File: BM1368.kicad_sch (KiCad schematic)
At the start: 38 parts, among them U2 BM1368_mode1, U9 BM1368_mode1

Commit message: Added 4th Phase Buck
Started to add 4th Phase for the Buck, implementing BM1370 footprint etc
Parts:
- removed U2, U9: BM1368_mode1, myfootprints:bm1368-package-modified, symbol mylib7:BM1368_mode1
- added U17, U2: BM1370_mode1, Nerd8:BM1370, symbol bitaxe:BM1370_mode1
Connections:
- net +0V8: now also U17.14 (VDDIO_08_0), U17.17 (VDDIO_08_1), U2.14 (VDDIO_08_0), U2.17 (VDDIO_08_1)
- net +1V2: now also U17.31 (VDD), U2.31 (VDD)
- net +1V8: now also U17.15 (VDDIO_12_0), U17.16 (VDDIO_12_1), U2.15 (VDDIO_12_0), U2.16 (VDDIO_12_1)
- net BI: now also U17.9 (BI)
- net BO: now also U2.22 (BO)
- net CI: now also U17.6 (CI)
- net CLKI: now also U17.8 (CLKI)
- net CLKO: now also U2.23 (CLKO)
- net CO: now also U2.25 (CO)
- net GND: now also U17.13 (PLL_VSS), U17.18 (VSS), U17.27 (VSS), U17.32 (VSS), U17.4 (VSS), U2.13 (PLL_VSS), U2.18 (VSS), U2.27 (VSS), U2.32 (VSS), U2.4 (VSS)
- net NRSTI: now also U17.5 (NRSTI)
- net NRSTO: now also U2.26 (NRSTO)
- net RI: now also U2.24 (RI)
- net RO: now also U17.7 (RO)
- net U9-VDD1_1: now also U2.28 (VDD1_1)
- net U9-VDD2_1: now also U2.29 (VDD2_1)
- net U9-VDD3_1: now also U2.30 (VDD3_1)
- net at C197.2, C50.2, C51.1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: now also U17.30 (VDD3_1), U2.1 (VDD3_0)
- net at C196.2, C197.1, C51.2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: now also U17.29 (VDD2_1), U2.2 (VDD2_0)
- net at C195.2, C196.1, C56.2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: now also U17.28 (VDD1_1), U2.3 (VDD1_0)
- net at R14.1: now also U2.11 (LITE_PAD)
- net at R11.2: now also U17.26 (NRSTO), U2.5 (NRSTI)
- net at R10.1: now also U17.24 (RI), U2.7 (RO)
- net at C42.2, C43.1: now also U17.1 (VDD3_0)
- net at R9.1: now also U17.11 (LITE_PAD)
- net at C36.2, C42.1: now also U17.2 (VDD2_0)
- net at C35.2, C36.1: now also U17.3 (VDD1_0)
- new net: U17.25 (CO), U2.6 (CI)
- new net: U17.23 (CLKO), U2.8 (CLKI)
- new net: U17.22 (BO), U2.9 (BI)

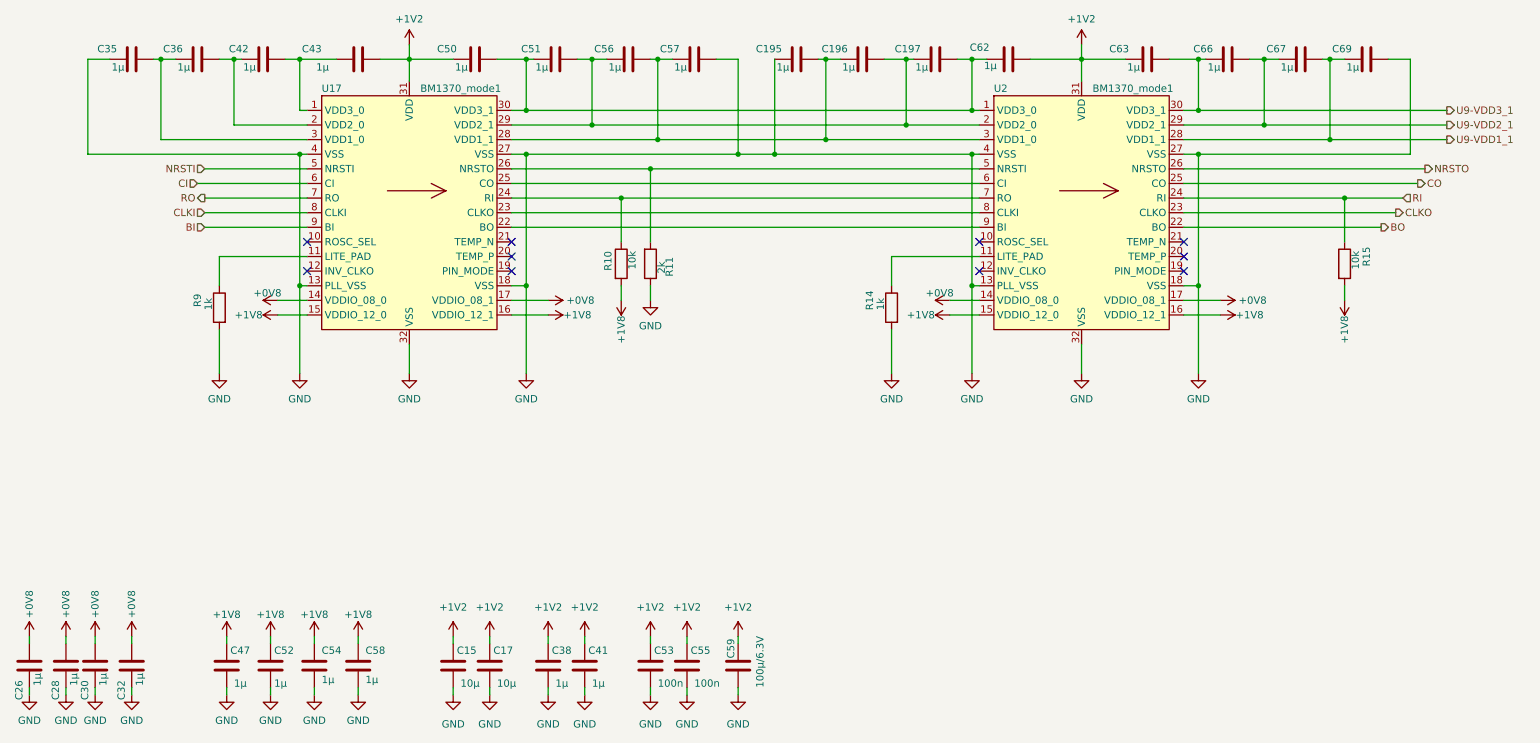
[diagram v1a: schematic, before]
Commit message: Changed LDO to 1V2 and original 1V2 to VDD
1V8 LDO replaced with 1V2 LDO
Crystal replaced
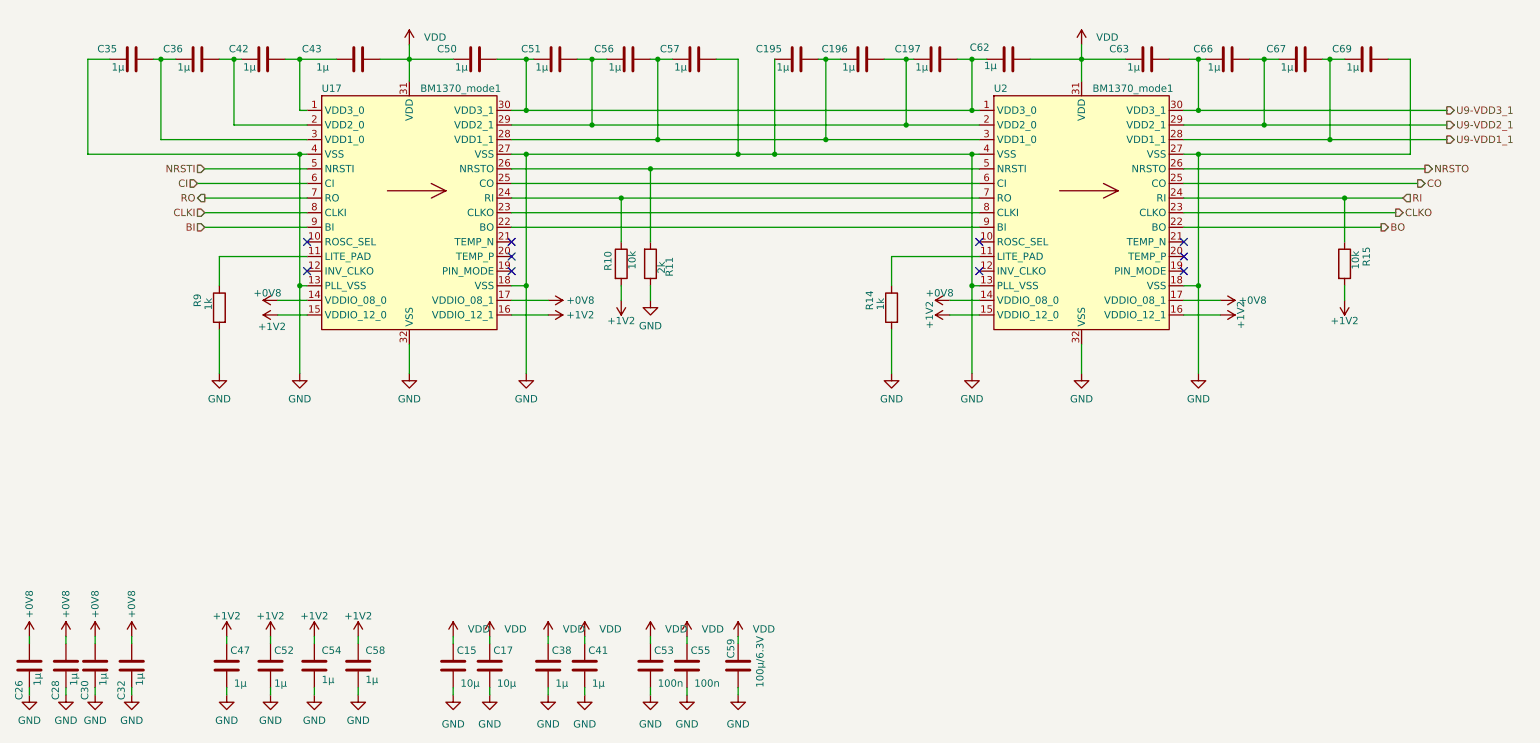
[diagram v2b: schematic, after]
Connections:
- net +1V8 is gone; now on net +1V2: C47.1, C52.1, C54.1, C58.1, R10.2, R15.2, U17.15 (VDDIO_12_0), U17.16 (VDDIO_12_1), U2.15 (VDDIO_12_0), U2.16 (VDDIO_12_1)
- net +1V2: no longer C15.1, C17.1, C38.1, C41.1, C43.2, C50.1, C53.1, C55.1, C59.1, C62.2, C63.1, U17.31 (VDD), U2.31 (VDD)
- new net VDD: C15.1, C17.1, C38.1, C41.1, C43.2, C50.1, C53.1, C55.1, C59.1, C62.2, C63.1, U17.31 (VDD), U2.31 (VDD)

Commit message: BOM changes
1nF  to 1nF 0.7mm etc
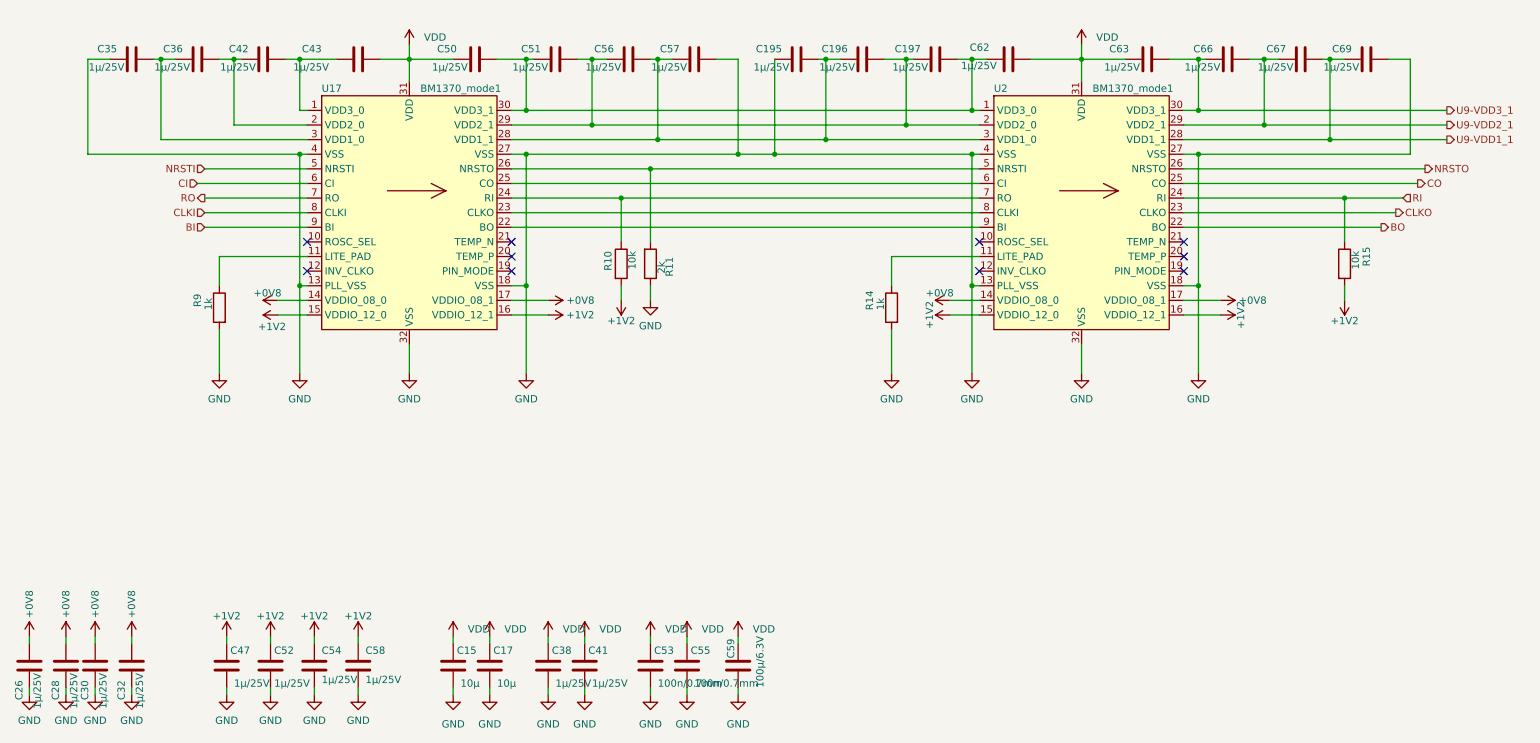
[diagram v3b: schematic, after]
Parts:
- C195, C196, C197, C26, C28, C30, C32, C35, C36, C38, C41, C42, C43, C47, C50, C51, C52, C54, C56, C57, C58, C62, C63, C66, C67, C69: value 1µ -> 1µ/25V; Distributor (none) -> D; Manufacturer (none) -> CL21B105KAFNNNE; OrderNr (none) -> 1276-1066-1-ND
- C53, C55: value 100n -> 100n/0.7mm; Distributor (none) -> D; Manufacturer (none) -> AC0805KRX7R9BB104; OrderNr (none) -> 311-3037-1-ND
- R10, R15: Distributor (none) -> D; Manufacturer (none) -> RMCF0805FT10K0; OrderNr (none) -> RMCF0805FT10K0CT-ND
- R11: Distributor (none) -> D; Manufacturer (none) -> CRG0805F2K0; OrderNr (none) -> A126358CT-ND
- R14, R9: Distributor (none) -> D; Manufacturer (none) -> RNCP0805FTD1K00; OrderNr (none) -> RNCP0805FTD1K00CT-ND
- U17, U2: Manufacturer (none) -> BM1370 BITMAIN; OrderNr (none) -> -
